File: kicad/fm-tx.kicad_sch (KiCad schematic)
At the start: 22 parts, among them J1 Conn_Coaxial, J2 Conn_Coaxial, J3 Conn_Coaxial, J4 Conn_Coaxial, SW1 RotaryEncoder_Switch, U1 esp32_38_pins-custom_library

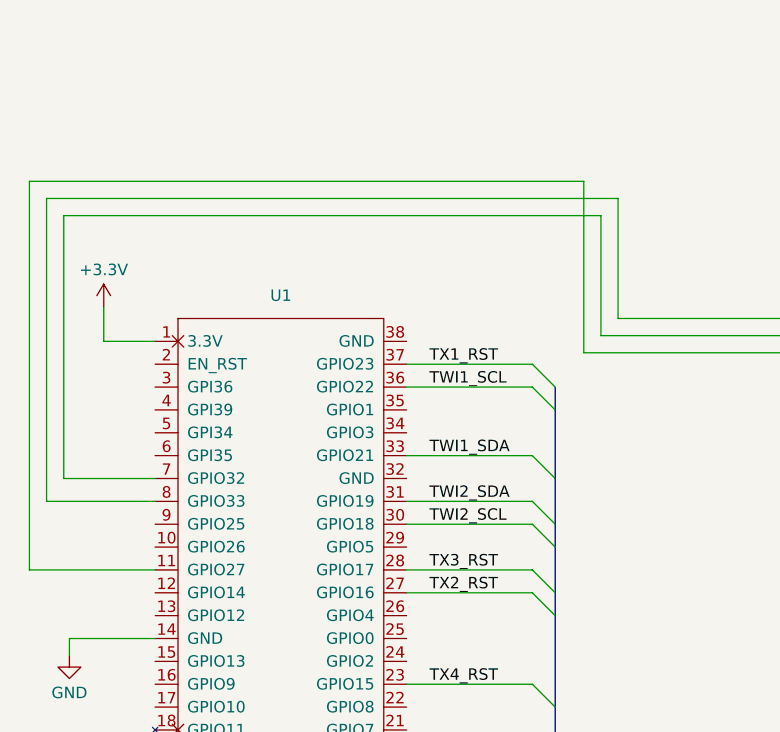
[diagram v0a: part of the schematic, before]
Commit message: update schematic
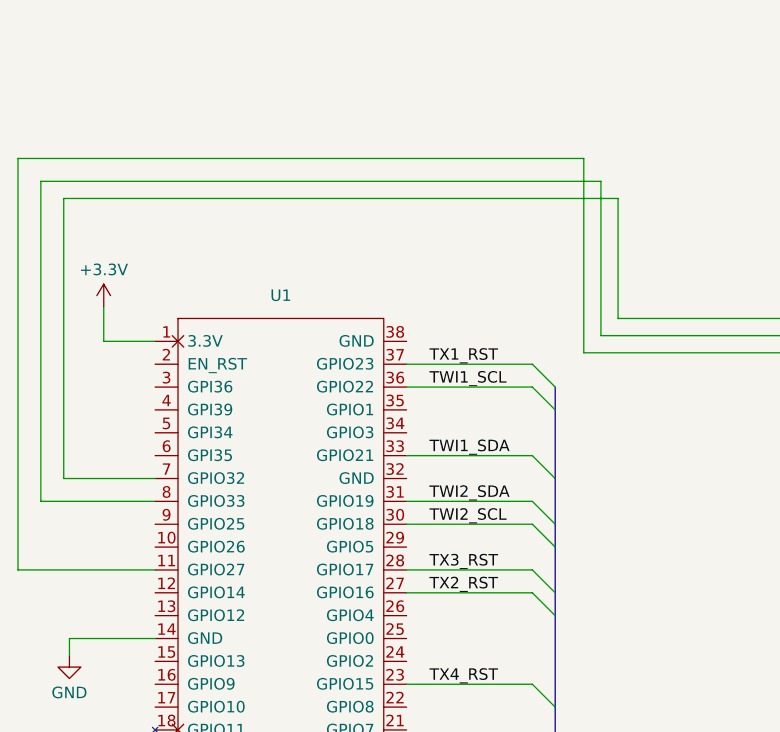
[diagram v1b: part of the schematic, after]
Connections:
- new net: U8. (VCC), U9. (VCC) (x2)
- new net: U6. (VCC), U7. (VCC) (x2)
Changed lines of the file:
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@@
 	(wire
 		(pts
-			(xy 38.1 69.85) (xy 26.035 69.85)
+			(xy 27.94 67.31) (xy 27.94 36.195)
 		)
 		(stroke
@@
 	(wire
 		(pts
-			(xy 38.1 67.31) (xy 27.94 67.31)
-		)
-		(stroke
-			(width 0)
-			(type default)
-		)
-	)
-	(wire
-		(pts
 			(xy 120.65 132.715) (xy 120.65 133.985)
 		)
@@
 	(wire
 		(pts
-			(xy 85.725 53.34) (xy 85.725 34.29)
+			(xy 85.725 53.34) (xy 85.725 31.75)
 		)
 		(stroke
@@
 	(wire
 		(pts
-			(xy 87.63 38.1) (xy 87.63 51.435)
+			(xy 87.63 34.29) (xy 87.63 51.435)
 		)
 		(stroke
@@
 	(wire
 		(pts
+			(xy 25.4 69.85) (xy 38.1 69.85)
+		)
+		(stroke
+			(width 0)
+			(type default)
+		)
+	)
+	(wire
+		(pts
 			(xy 127 78.105) (xy 127 80.01)
 		)
@@
 	(wire
 		(pts
-			(xy 24.13 77.47) (xy 24.13 34.29)
+			(xy 22.86 77.47) (xy 22.86 31.75)
 		)
 		(stroke
@@
 	(wire
 		(pts
-			(xy 26.035 36.195) (xy 89.535 36.195)
+			(xy 27.94 36.195) (xy 89.535 36.195)
 		)
 		(stroke
@@
 	(wire
 		(pts
-			(xy 26.035 69.85) (xy 26.035 36.195)
-		)
-		(stroke
-			(width 0)
-			(type default)
-		)
-	)
-	(wire
-		(pts
 			(xy 240.665 43.815) (xy 240.665 52.07)
 		)
@@
 		)
 	)
+	(wire
+		(pts
+			(xy 27.94 67.31) (xy 38.1 67.31)
+		)
+		(stroke
+			(width 0)
+			(type default)
+		)
+	)
 	(bus
 		(pts
@@
 	(wire
 		(pts
-			(xy 24.13 34.29) (xy 85.725 34.29)
+			(xy 22.86 31.75) (xy 85.725 31.75)
 		)
 		(stroke
@@
 	(wire
 		(pts
-			(xy 27.94 38.1) (xy 87.63 38.1)
+			(xy 25.4 34.29) (xy 87.63 34.29)
 		)
 		(stroke
@@
 	(wire
 		(pts
-			(xy 24.13 77.47) (xy 38.1 77.47)
+			(xy 22.86 77.47) (xy 38.1 77.47)
 		)
 		(stroke
@@
 	(wire
 		(pts
-			(xy 27.94 67.31) (xy 27.94 38.1)
-		)
-		(stroke
+			(xy 25.4 34.29) (xy 25.4 69.85)
+		)
+		(stroke
